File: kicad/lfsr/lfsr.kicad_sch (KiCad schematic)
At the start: 25 parts, among them SW1 SW_Push, SW2 SW_Push, U1 74HC164, U2 74HC86, U3 LM7805_TO220, U4 LM555xN

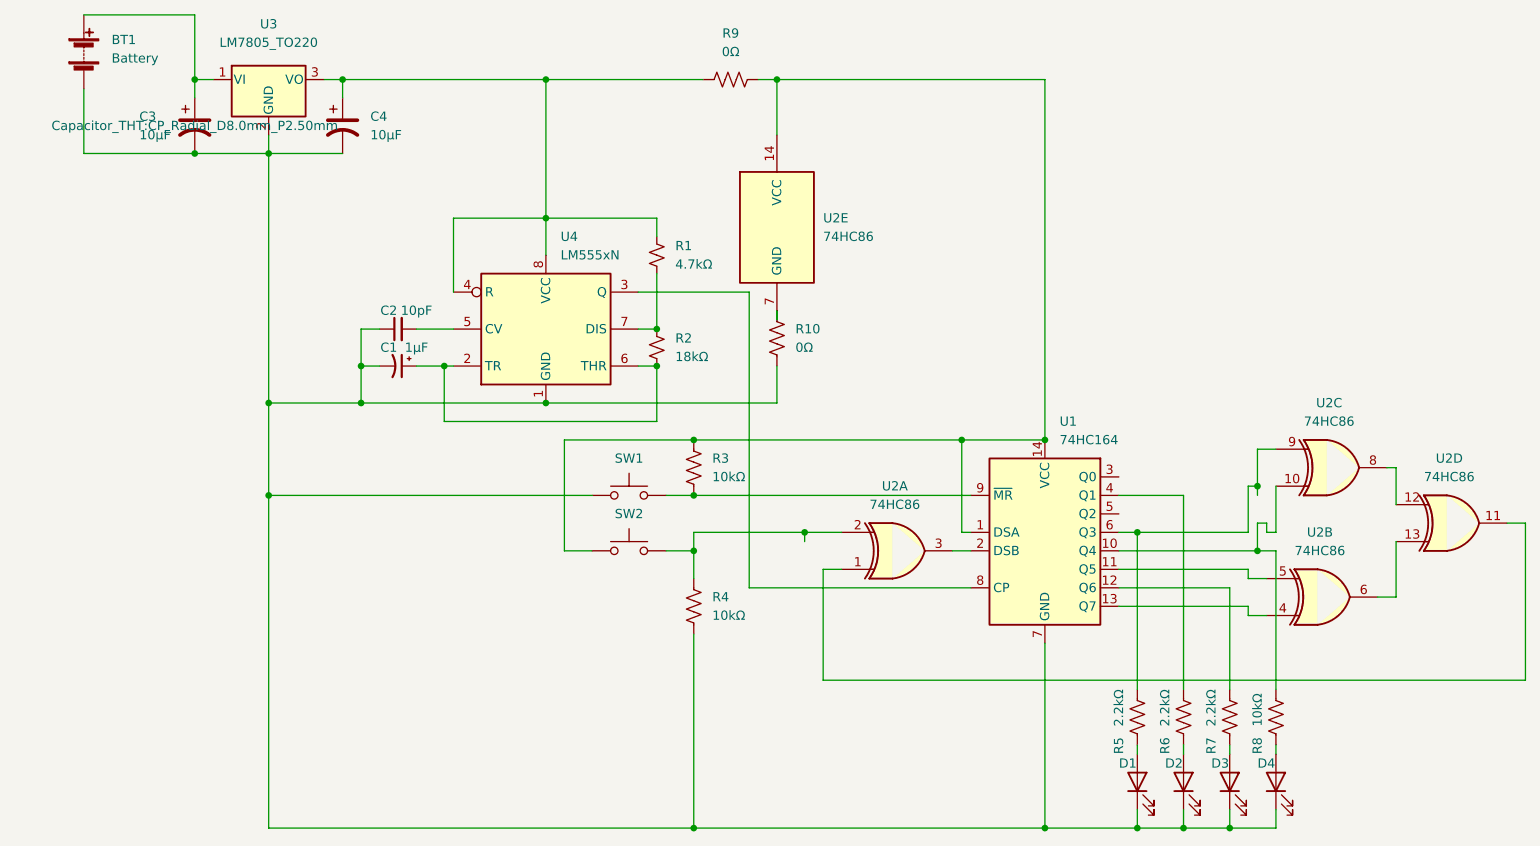
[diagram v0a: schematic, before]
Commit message: Modify PCB design
Swap things around so that traces are a minimum of 1mm wide instead of 0.1mm wide. 0.1mm traces didn't perform well on the router
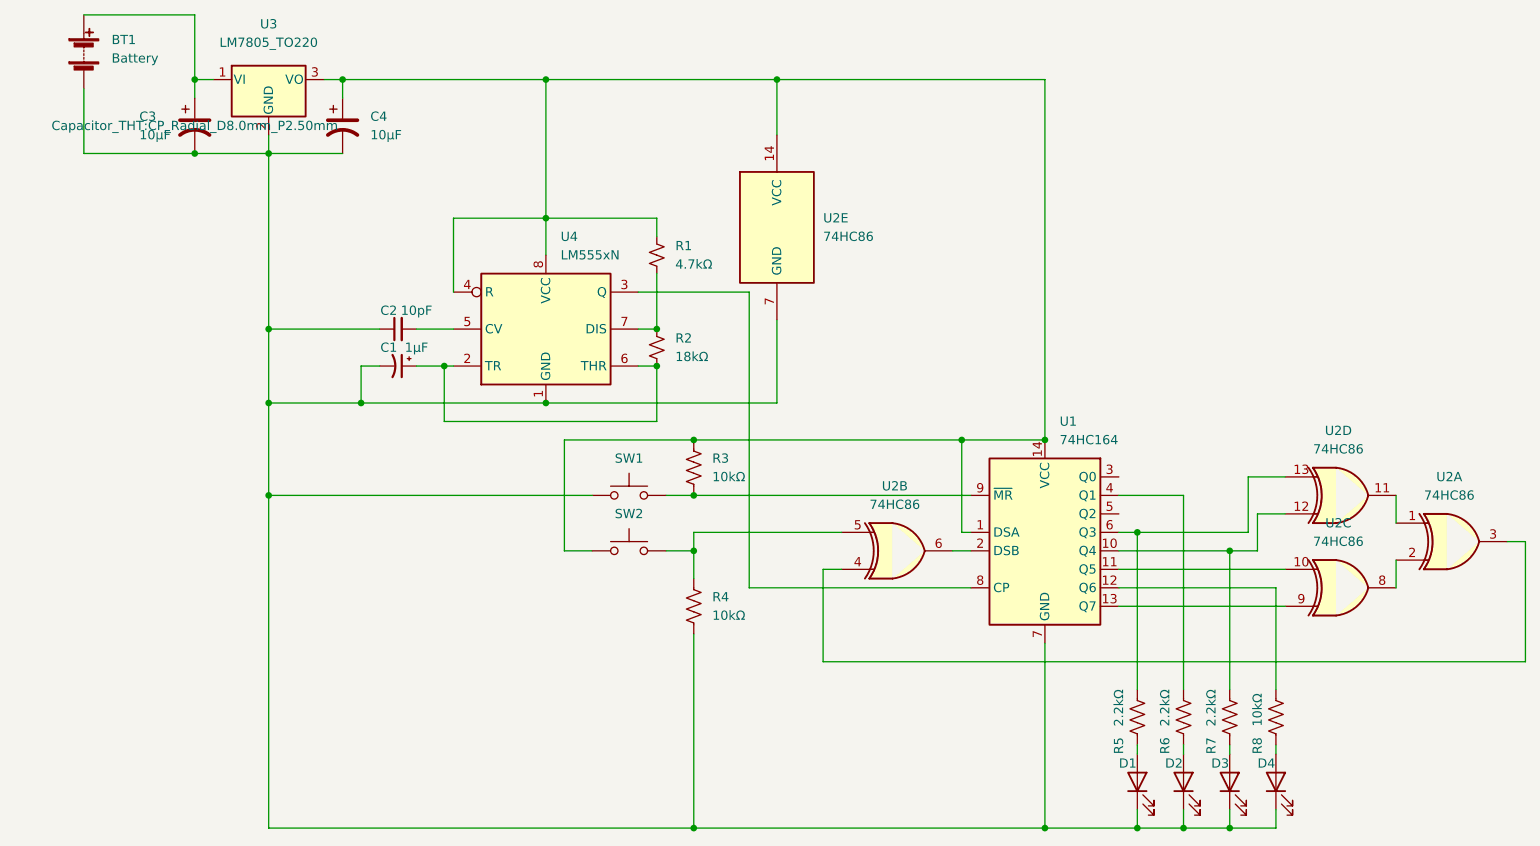
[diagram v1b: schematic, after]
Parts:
- removed R10: 0Ω, Resistor_THT:R_Axial_DIN0207_L6.3mm_D2.5mm_P10.16mm_Horizontal, symbol Device:R_US
- removed R9: 0Ω, Resistor_THT:R_Axial_DIN0207_L6.3mm_D2.5mm_P7.62mm_Horizontal, symbol Device:R_US
- R1, R2: footprint Resistor_THT:R_Axial_DIN0207_L6.3mm_D2.5mm_P10.16mm_Horizontal -> Resistor_THT:R_Axial_DIN0207_L6.3mm_D2.5mm_P2.54mm_Vertical
- R4: footprint Resistor_THT:R_Axial_DIN0207_L6.3mm_D2.5mm_P10.16mm_Horizontal -> Resistor_THT:R_Axial_DIN0204_L3.6mm_D1.6mm_P7.62mm_Horizontal
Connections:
- net at BT1.2 (-), C1.2, C2.1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: now also U2.7 (GND)
- net at U2.12: now also R7.1, U1.10 (Q4); no longer U2.8
- net at U2.13: now also R5.1, U1.6 (Q3); no longer U2.6
- net at C4.1, R1.1, U3.3 (VO)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: now also R3.1, SW2.1, U1.1 (DSA), U1.14 (VCC), U2.14 (VCC)
- net at U1.11 (Q5): now also U2.10; no longer U2.5
- net at U1.12 (Q6): now also R8.1; no longer R7.1
- net at U1.13 (Q7): now also U2.9; no longer U2.4
- net at U1.2 (DSB): now also U2.6; no longer U2.3
- net at R4.1, SW2.2: now also U2.5; no longer U2.2
- new net: U2.2, U2.8
- new net: U2.3, U2.4
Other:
- moved on the sheet: U2A, U2B, U2C, U2D
